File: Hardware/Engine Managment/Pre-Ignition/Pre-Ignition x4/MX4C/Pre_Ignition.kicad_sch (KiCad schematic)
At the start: 0 parts

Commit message: Upload correct initial upload files
Initial upload files were accidently taken from an alpha folder. 5v pins on main connector had no voltage. To fix the issue on any manufactured boards remove C8 and C9. Then short the pins of the removed capacitors.
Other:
- note added: "Rev C2"
- note added: "© 2023 DetonationEMS (Aaron S.)"
- note removed: "Rev C"
- note removed: "© 2022 DetonationEMS (Aaron S.)"

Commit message: Structure Update
MX2 - RevB Upload
MX4B-2 - KiCad Version update (no changes)
MX4C - Organized Schematic, Minor layout change
Engine Simulator 8 Channel - Organized Schematic (no changes)
PMAP-M - Map Sensor Breakout for MX4C
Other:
- note added: "Spark Gap x4 is a 4 channel, (4 indavidually controlled ignition and injector outputs) universal standalone engine managment system. Board Selection in tuner studio for this ECU is "Speeduino v0.4""
- note removed: "Pre-Ignition x4 is a 4 channel, (4 indavidually controlled ignition and injector outputs) Universal Standalone Engine Managment System."
- note removed: "Rev C2"
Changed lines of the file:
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@@
   (title_block
     (title "Pre-Ignition X4")
-    (date "2023-05-11")
-    (rev "C2")
+    (date "2023-06-15")
+    (rev "C")
     (company "DetonationEMS")
     (comment 1 "detonationems.com")
   )
-  (text "Pre-Ignition x4 is a 4 channel, (4 indavidually controlled ignition and injector outputs)\nUniversal Standalone Engine Managment System."
-    (at 57.15 69.85 0)
+  (text "Spark Gap x4 is a 4 channel, (4 indavidually controlled ignition and injector outputs)\nuniversal standalone engine managment system. \n\nBoard Selection in tuner studio for this ECU is \"Speeduino v0.4\""
+    (at 57.15 77.47 0)
     (effects (font (size 2.54 2.54)) (justify left bottom))
   )
@@
     (effects (font (size 2.54 2.54)) (justify left bottom))
   )
-  (text "Rev C2" (at 99.06 39.37 0)
-    (effects (font (size 2.54 2.54)) (justify left bottom))
-  )

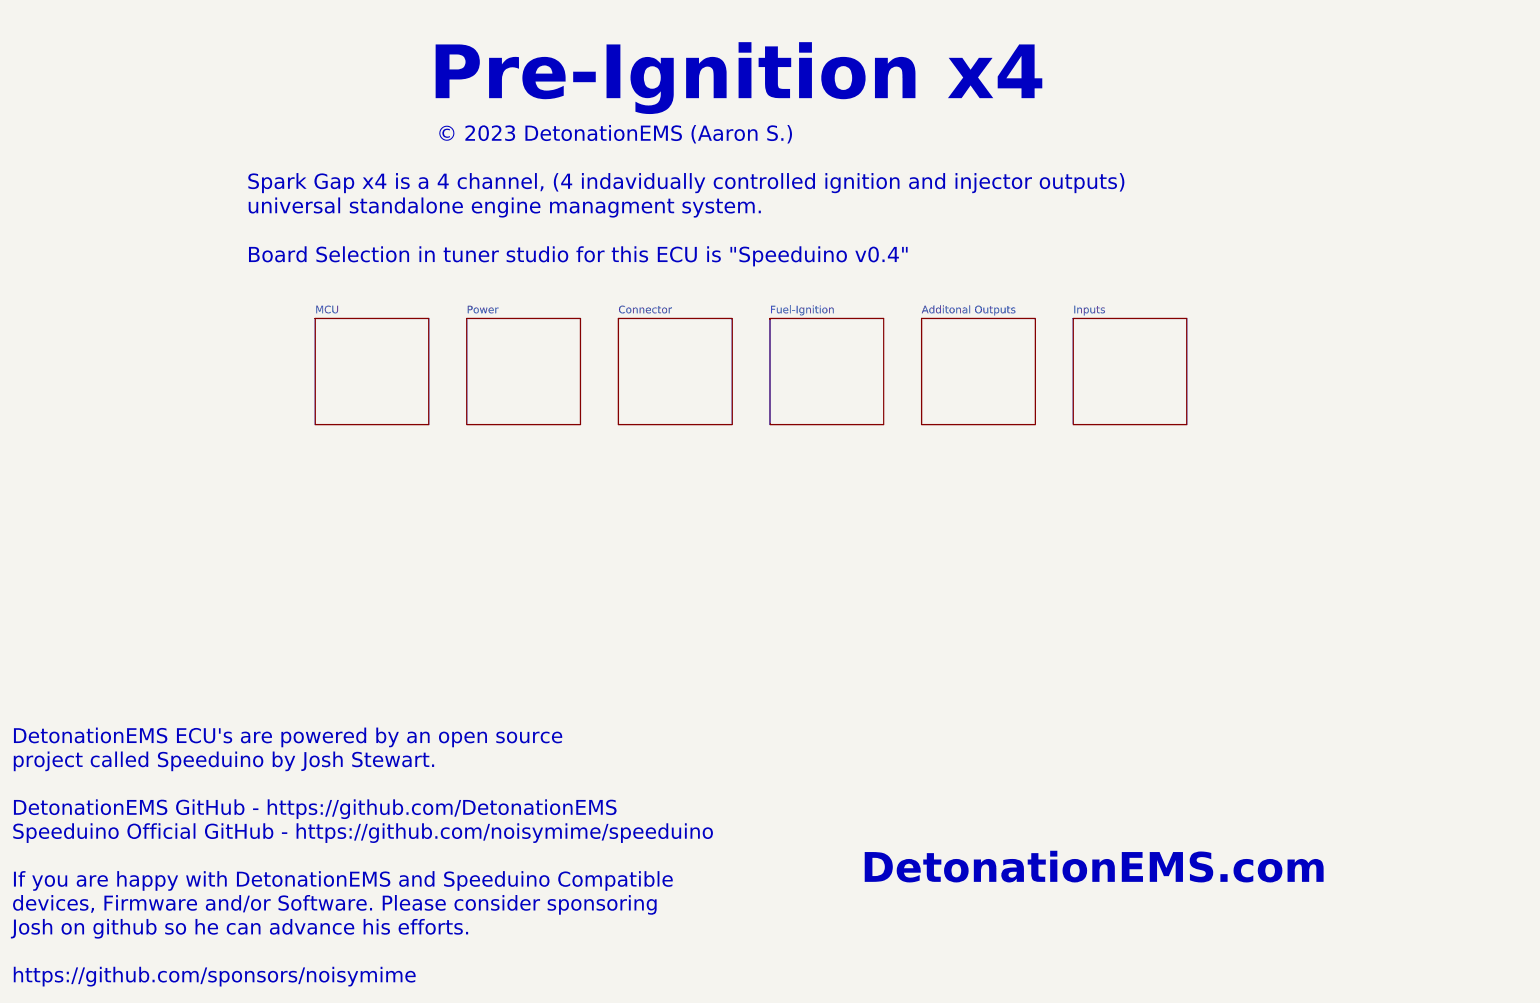
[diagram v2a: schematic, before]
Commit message: minor update
Copper Pour and clearances updated.
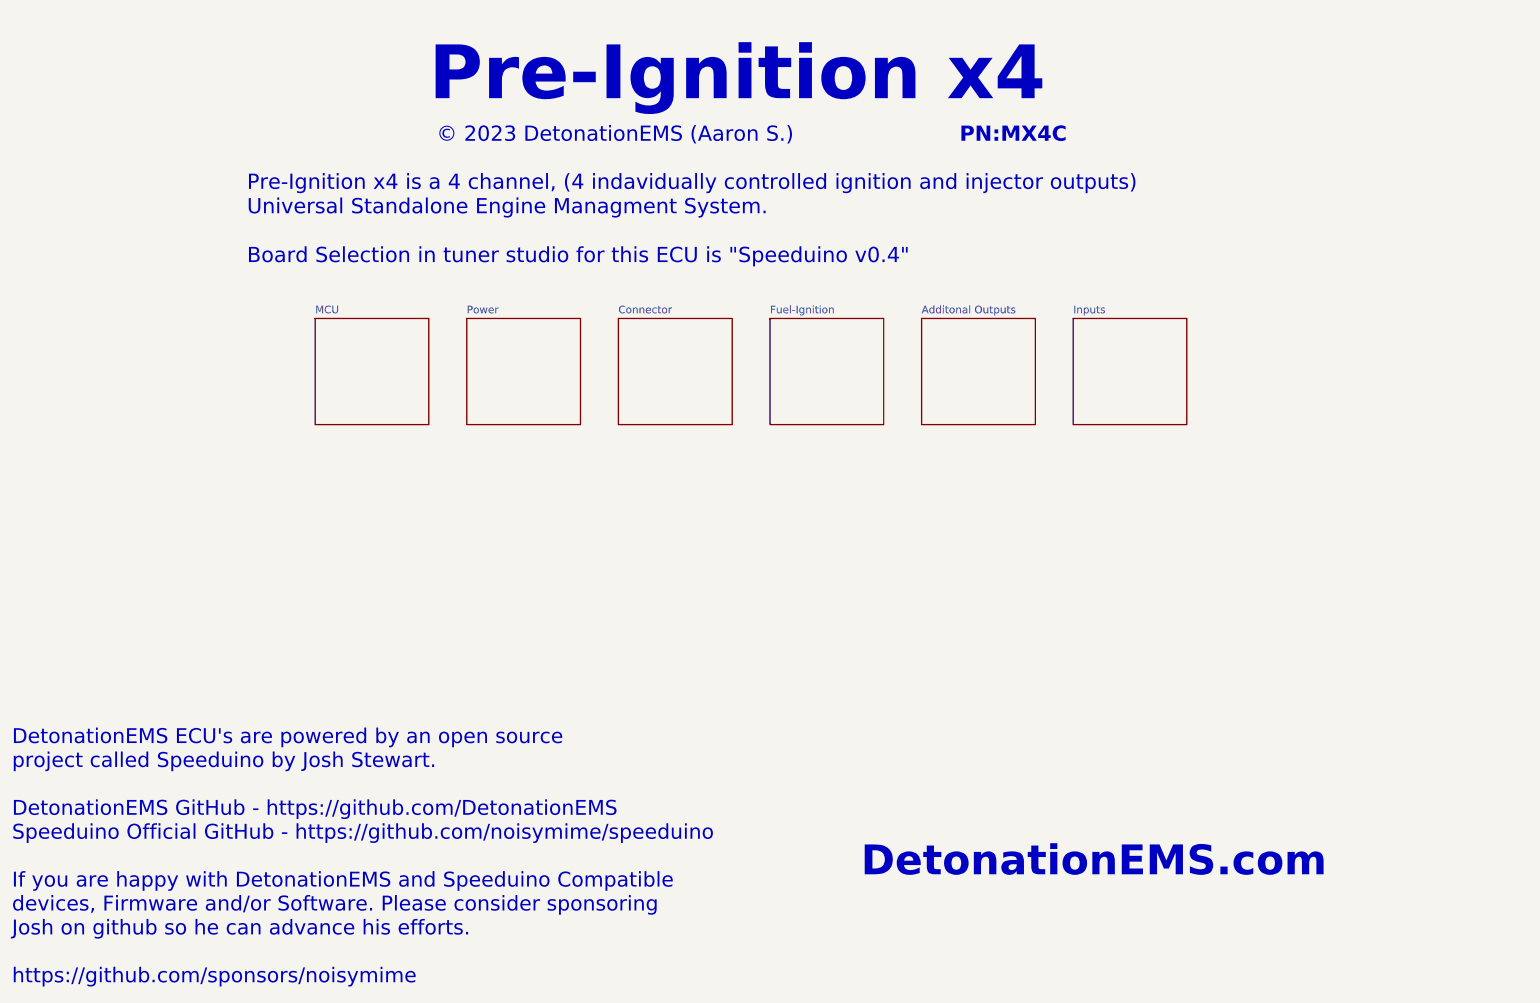
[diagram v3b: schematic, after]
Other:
- note added: "PN:MX4C"
- note added: "Pre-Ignition x4 is a 4 channel, (4 indavidually controlled ignition and injector outputs) Universal Standalone Engine Managment System. Board Selection in tuner studio for this ECU is "Speeduino v0.4""
- note removed: "Spark Gap x4 is a 4 channel, (4 indavidually controlled ignition and injector outputs) universal standalone engine managment system. Board Selection in tuner studio for this ECU is "Speeduino v0.4""
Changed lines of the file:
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@@
   (title_block
     (title "Pre-Ignition X4")
-    (date "2023-06-15")
+    (date "2023-10-24")
     (rev "C")
     (company "DetonationEMS")
     (comment 1 "detonationems.com")
   )
-  (text "Spark Gap x4 is a 4 channel, (4 indavidually controlled ignition and injector outputs)\nuniversal standalone engine managment system. \n\nBoard Selection in tuner studio for this ECU is \"Speeduino v0.4\""
+  (text "Pre-Ignition x4 is a 4 channel, (4 indavidually controlled ignition and injector outputs)\nUniversal Standalone Engine Managment System.\n\nBoard Selection in tuner studio for this ECU is \"Speeduino v0.4\""
     (at 57.15 77.47 0)
     (effects (font (size 2.54 2.54)) (justify left bottom))
@@
     (effects (font (size 9 9) (thickness 1.8) bold) (justify left bottom))
   )
-  (text "DetonationEMS.com" (at 160.02 181.61 0)
+  (text "DetonationEMS.com" (at 160.02 180.34 0)
     (effects (font (size 5 5) (thickness 1) bold) (justify left bottom))
   )
@@
     (effects (font (size 2.4892 2.4892)) (justify left bottom))
   )
+  (text "PN:MX4C" (at 176.53 57.15 0)
+    (effects (font (size 2.54 2.54) (thickness 0.7) bold) (justify left bottom))
+  )
   (sheet (at 119.38 86.36) (size 19.05 17.78) (fields_autoplaced)
